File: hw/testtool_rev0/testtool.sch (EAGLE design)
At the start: 495 parts, among them IC1 SJA1105TELY, IC10 TJA1100HNZ, IC11 KSZ8061MNXI-TR, IC12 TJA1100HNZ, IC13 TLE9250XSJXUMA1, IC17 LP5907QMFX-3.3Q1, IC18 TLE9250XSJXUMA1, IC2 ATSAMV71Q21B-AABT, IC3 TJA1100HNZ, IC4 FT2232HL, IC5 TRS3232EQPWRQ1, IC6 SST26VF032BT-104I_SM, IC7 DS3231SN#, IC8 74HC7541D-Q100J, IC9 TPS62242DRVR, J10 5-2337992-3, J11 2301843-1, J12 1017505, J13 2301843-1, J15 693022010811, J2 2305018-2, J27 2041119-2, J3 1017505, J4 1017505, J5 1017505, J6 1017505, J7 1017505, J8 1017505, J9 1017505, U1 122-2920-GR, U2 LM63625, U3 TPS62007-Q1_DGS_10, Y1 NX3225SA-25MHZ-EXS00A-CS11338, Y3 ABM8AIG-12.000MHZ-1Z-T

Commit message: Add schematic for test tool based on the full vehicle control module design
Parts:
- removed C104: 10uF, rcl:C-USC0805
- removed C108, C111, C114, C116, C118, C120, C122, C124, C126, C128, C130, C132, C134, C136, C138, C140, C142, C144, C148, C149, C150, C151, C152, C153, C154, C155: 0.01uF, rcl:C-USC0603
- removed C109, C35, C36, C38, C42, C51, C52, C54, C58, C64, C65, C96: 1uF, rcl:C-USC0603
- removed C110, C21, C24, C26, C27, C29, C79, C80, C81, C82, C89: 0.1uF, rcl:C-USC0603
- removed C112, C113, C115, C117, C119, C121, C123, C125, C127, C129, C131, C133, C135, C137, C139, C141, C143, C145: 150nF, rcl:C-USC0603
- removed C22: 1000pF, rcl:C-USC0603
- removed C23, C25, C28, C32, C34, C39, C48, C50, C55: 10uF, rcl:C-USC0603
- removed C33, C37, C40, C41, C45, C46, C49, C53, C56, C57, C61, C62, C98: 100nF, rcl:C-USC0603
- removed C43, C44, C59, C60: 47pF, rcl:C-USC0603
- removed C47, C63: 4.7nF, rcl:C-USC0603
- removed C97: UCZ1K151MNQ1MS, samacsys:UCZ1K151MNQ1MS
- removed D10, D11, D12, D13, D14, D15, D16, D17, D18, D19, D20, D21, D22, D23, D24, D25, D26, D27, D28, D29, D30, D31, D32, D33, D34, D35: BAT54SWFILMY, samacsys:BAT54SWFILMY
- removed D2, D3: PESD2ETH-AXR, samacsys:PESD2ETH-AXR
- removed FL10, FL11, FL12, FL6, FL7, FL8: BLM18PG330SN1D, samacsys:BLM18PG330SN1D
- removed FL5, FL9: ACT45L-201-2P-TL000, samacsys:ACT45L-201-2P-TL000
- removed IC10, IC12: TJA1100HNZ, samacsys:TJA1100HNZ
- removed IC11: KSZ8061MNXI-TR, samacsys:KSZ8061MNXI-TR
- removed IC17: LP5907QMFX-3.3Q1, samacsys:LP5907QMFX-3.3Q1
- removed IC5: TRS3232EQPWRQ1, samacsys:TRS3232EQPWRQ1
- removed IC6: SST26VF032BT-104I_SM, samacsys:SST26VF032BT-104I_SM
- removed IC7: DS3231SN#, samacsys:DS3231SN#
- removed IC8: 74HC7541D-Q100J, samacsys:74HC7541D-Q100J
- removed IC9: TPS62242DRVR, samacsys:TPS62242DRVR
- removed J10: 5-2337992-3, samacsys:5-2337992-3
- removed J11, J13: 2301843-1, samacsys:2301843-1
- removed J12, J7, J8, J9: 1017505, samacsys:1017505
- removed J15: 693022010811, samacsys:693022010811
- removed J27: 2041119-2, samacsys:2041119-2
- removed L10: LPS3015-222MRB, samacsys:LPS3015-222MRB
- removed L3, L4, L5, L6: 0603CS-R12XGLU, samacsys:0603CS-R12XGLU
- removed LED10, LED2, LED3, LED8, LED9: (no value), led:LEDCHIPLED_0603
- removed R100, R101, R102, R199, R36, R38, R42, R45, R47, R49, R58, R60, R64, R67, R69, R71, R84, R93: 10k, rcl:R-US_R0603
- removed R105, R106, R115, R120, R125, R130, R135, R140, R145, R150, R155, R160, R165, R170, R175, R180, R185, R190: 4, rcl:R-US_R1206
- removed R107, R110, R111, R113, R114, R116, R119, R121, R123, R124, R126, R129, R131, R133, R134, R136, R139, R141, R143, R144, R146, R149, R151, R153, R154, R156, R159, R161, R163, R164, R166, R169, R171, R173, R174, R176, R179, R181, R184, R186, R189, R191, R194, R198, R79, R80, R81: 4.7k, rcl:R-US_R0603
- removed R108, R112, R117, R122, R127, R132, R137, R142, R147, R152, R157, R162, R167, R172, R177, R182, R187, R192: 2.74k, rcl:R-US_R0603
- removed R109, R118, R128, R138, R148, R158, R168, R178, R55, R77: 100k, rcl:R-US_R0603
- removed R27, R28, R29: 75, rcl:R-US_R0603
- removed R30, R33, R35, R53, R54, R57, R75, R76: 1k, rcl:R-US_R0603
- removed R34, R50, R51, R52, R56, R72, R73, R74: 49.9, rcl:R-US_R0603
- removed R37, R39, R43, R44, R46, R48, R59, R61, R65, R66, R68, R70: DNP, rcl:R-US_R0603
- removed R40, R62: 5.11k, rcl:R-US_R0603
- removed R41, R63, R78, R99: 0, rcl:R-US_R0603
- removed R94: 1.21k, rcl:R-US_R0603
- removed U1: 122-2920-GR, samacsys:122-2920-GR
- removed U?1, U?10, U?11, U?12, U?13, U?14, U?15, U?16, U?17, U?18, U?2, U?3, U?4, U?5, U?6, U?7, U?8, U?9: (no value), BTS50015-1TAD:BTS50015-1TAD
- added J1: 2305018-2, 2305018-2:2305018-2
- C17: value 1uF -> 100nF
- C18: value 8.2pF -> 10uF; device rcl:C-USC0603 -> rcl:C-USC0805
- C20: value 0.1uF -> 8.2pF
- IC1: value SJA1105TELY -> SST26VF032BT-104I_SM; device samacsys:SJA1105TELY -> samacsys:SST26VF032BT-104I_SM
- J3, J4, J5, J6: value 1017505 -> TBL009-254-04GY-2GY; device samacsys:1017505 -> samacsys:TBL009-254-04GY-2GY
- R10, R25: value 0 -> 10k
- R11, R14: value 10k -> DNP
- R12, R13: value DNP -> 10k
- R26: value 75 -> 0
- R31: value 6.04k -> 5.11k
- R32: value 4.7k -> 5.11k
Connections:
- net PHY1_CONFIG0 renamed PHY_CONFIG0
- net PHY1_CONFIG1 renamed PHY_CONFIG1
- net PHY1_TRX_M renamed PHY_TRX_M
- net PHY1_TRX_P renamed PHY_TRX_P
- removed net 3V3_AD_REF: C109.1, IC17.OUT, IC2.VREFP, R100.1
- removed net ADC0_0: C89.1, IC2.PD30, R93.2, R94.2
- removed net ADC0_1: IC2.PA21
- removed net ADC0_10: C140.1, D25.A,K, IC2.PB0, R181.2
- removed net ADC0_3: C128.1, D19.A,K, IC2.PE5, R151.2
- removed net ADC0_4: C130.1, D20.A,K, IC2.PE4, R156.2
- removed net ADC0_6: C132.1, D21.A,K, IC2.PA17, R161.2
- removed net ADC0_7: C134.1, D22.A,K, IC2.PA18, R166.2
- removed net ADC0_8: C136.1, D23.A,K, IC2.PA19, R171.2
- removed net ADC0_9: C138.1, D24.A,K, IC2.PA20, R176.2
- removed net ADC1_0: C142.1, D26.A,K, IC2.PB1, R186.2
- removed net ADC1_1: C144.1, D27.A,K, IC2.PC13, R191.2
- removed net ADC1_10: C124.1, D17.A,K, IC2.PE3, R141.2
- removed net ADC1_11: C126.1, D18.A,K, IC2.PE0, R146.2
- removed net ADC1_2: C111.1, D10.A,K, IC2.PC15, R107.2
- removed net ADC1_4: C108.1, D11.A,K, IC2.PC29, R111.2
- removed net ADC1_5: C114.1, D12.A,K, IC2.PC30, R116.2
- removed net ADC1_6: C116.1, D13.A,K, IC2.PC31, R121.2
- removed net ADC1_7: C118.1, D14.A,K, IC2.PC26, R126.2
- removed net ADC1_8: C120.1, D15.A,K, IC2.PC27, R131.2
- removed net ADC1_9: C122.1, D16.A,K, IC2.PC0, R136.2
- removed net CON_ETH1_TRX_M: C14.2, R22.2
- removed net CON_ETH1_TRX_P: C15.2, R23.2
- removed net CON_ETH2_TRX_M: C45.2, R53.2
- removed net CON_ETH2_TRX_P: C46.2, R54.2
- removed net CON_ETH3_TRX_M: C61.2, R75.2
- removed net CON_ETH3_TRX_P: C62.2, R76.2
- removed net DEBUG_ETH_CONFIG1: IC11.CRS, R32.2
- removed net DEBUG_ETH_LED0: IC11.LED0/TXER, R30.1
- removed net DEBUG_ETH_LED1: IC11.SIGDET, R33.1
- removed net DEBUG_ETH_RXM: IC11.RXM, J10.P6
- removed net DEBUG_ETH_RXP: IC11.RXP, J10.P3
- removed net DEBUG_ETH_TXM: IC11.TXM, J10.P2
- removed net DEBUG_ETH_TXP: IC11.TXP, J10.P1
- removed net EXTINT_RTC: IC2.PA0, IC7.!INT!/SQW, R81.1
- removed net EXT_DINPUT_0: R198.1
- removed net EXT_DINPUT_1: R113.1
- removed net EXT_DINPUT_2: R123.1
- removed net EXT_DINPUT_3: R133.1
- removed net EXT_DINPUT_4: R143.1
- removed net EXT_DINPUT_5: R153.1
- removed net EXT_DINPUT_6: R163.1
- removed net EXT_DINPUT_7: R173.1
- removed net EXT_PWR: D5.A, D9.A, TC1.5
- removed net HIGHSIDE_0_EN: IC2.PD11, R154.2
- removed net HIGHSIDE_0_OUTPUT: U?10.OUT1, U?10.OUT2, U?10.OUT3
- removed net HIGHSIDE_10_EN: IC2.PC2, R114.2
- removed net HIGHSIDE_10_OUTPUT: U?2.OUT1, U?2.OUT2, U?2.OUT3
- removed net HIGHSIDE_11_EN: IC2.PC3, R119.2
- removed net HIGHSIDE_11_OUTPUT: U?3.OUT1, U?3.OUT2, U?3.OUT3
- removed net HIGHSIDE_12_EN: IC2.PA16, R124.2
- removed net HIGHSIDE_12_OUTPUT: U?4.OUT1, U?4.OUT2, U?4.OUT3
- removed net HIGHSIDE_13_EN: IC2.PD27, R129.2
- removed net HIGHSIDE_13_OUTPUT: U?5.OUT1, U?5.OUT2, U?5.OUT3
- removed net HIGHSIDE_14_EN: IC2.PC7, R134.2
- removed net HIGHSIDE_14_OUTPUT: U?6.OUT1, U?6.OUT2, U?6.OUT3
- removed net HIGHSIDE_15_EN: IC2.PA15, R139.2
- removed net HIGHSIDE_15_OUTPUT: U?7.OUT1, U?7.OUT2, U?7.OUT3
- removed net HIGHSIDE_16_EN: IC2.PC6, R144.2
- removed net HIGHSIDE_16_OUTPUT: U?8.OUT1, U?8.OUT2, U?8.OUT3
- removed net HIGHSIDE_17_EN: IC2.PD24, R149.2
- removed net HIGHSIDE_17_OUTPUT: U?9.OUT1, U?9.OUT2, U?9.OUT3
- removed net HIGHSIDE_1_EN: IC2.PA2, R159.2
- removed net HIGHSIDE_1_OUTPUT: U?11.OUT1, U?11.OUT2, U?11.OUT3
- removed net HIGHSIDE_2_EN: IC2.PA25, R164.2
- removed net HIGHSIDE_2_OUTPUT: U?12.OUT1, U?12.OUT2, U?12.OUT3
- removed net HIGHSIDE_3_EN: IC2.PA7, R169.2
- removed net HIGHSIDE_3_OUTPUT: U?13.OUT1, U?13.OUT2, U?13.OUT3
- removed net HIGHSIDE_4_EN: IC2.PA31, R174.2
- removed net HIGHSIDE_4_OUTPUT: U?14.OUT1, U?14.OUT2, U?14.OUT3
- removed net HIGHSIDE_5_EN: IC2.PA8, R179.2
- removed net HIGHSIDE_5_OUTPUT: U?15.OUT1, U?15.OUT2, U?15.OUT3
- removed net HIGHSIDE_6_EN: IC2.PA23, R184.2
- removed net HIGHSIDE_6_OUTPUT: U?16.OUT1, U?16.OUT2, U?16.OUT3
- removed net HIGHSIDE_7_EN: IC2.PE1, R189.2
- removed net HIGHSIDE_7_OUTPUT: U?17.OUT1, U?17.OUT2, U?17.OUT3
- removed net HIGHSIDE_8_EN: IC2.PE2, R194.2
- removed net HIGHSIDE_8_OUTPUT: U?18.OUT1, U?18.OUT2, U?18.OUT3
- removed net HIGHSIDE_9_EN: IC2.PC1, R110.2
- removed net HIGHSIDE_9_OUTPUT: U?1.OUT1, U?1.OUT2, U?1.OUT3
- removed net I2C0_TWCK: IC2.PA4, IC7.SCL, R79.1
- removed net I2C0_TWD: IC2.PA3, IC7.SDA, R80.1
- removed net MII4_RXD0: IC1.MII4_RX0, IC11.RXD0
- removed net MII4_RXD1: IC1.MII4_RX1, IC11.RXD1
- removed net MII4_RXD2: IC1.MII4_RX2, IC11.RXD2
- removed net MII4_RXD3: IC1.MII4_RX3, IC11.RXD3
- removed net MII4_RXERR: IC11.RXERR
- removed net MII4_RX_CLK: IC1.MII4_RX_CLK, IC11.RXC
- removed net MII4_RX_DV: IC1.MII4_RX_DV, IC11.RXDV
- removed net MII4_RX_ER: IC1.MII4_RX_ER
- removed net MII4_TXD0: IC1.MII4_TXD0, IC11.TXD0
- removed net MII4_TXD1: IC1.MII4_TXD1, IC11.TXD1
- removed net MII4_TXD2: IC1.MII4_TXD2, IC11.TXD2
- removed net MII4_TXD3: IC1.MII4_TXD3, IC11.TXD3
- removed net MII4_TXEN: IC1.MII4_TXEN, IC11.TXEN
- removed net MII4_TX_CLK: IC1.MII3_TX_ER_1, IC11.TXC
- removed net MODEM_DISABLE: IC2.PB9, J27.W_DISABLE#
- removed net MODEM_RESET: IC2.PB8, J27.PERST#
- removed net MODEM_WAN_LED: J27.LED_WWAN#, LED9.C
- removed net N$100: C115.2, R115.1, U?3.GND
- removed net N$101: R116.1, R117.1, U?3.IS
- removed net N$102: C115.1, R119.1, U?3.IN
- removed net N$103: C117.2, R120.1, U?4.GND
- removed net N$104: R121.1, R122.1, U?4.IS
- removed net N$105: C117.1, R124.1, U?4.IN
- removed net N$106: C119.2, R125.1, U?5.GND
- removed net N$107: R126.1, R127.1, U?5.IS
- removed net N$108: C119.1, R129.1, U?5.IN
- removed net N$109: C121.2, R130.1, U?6.GND
- removed net N$110: R131.1, R132.1, U?6.IS
- removed net N$111: C121.1, R134.1, U?6.IN
- removed net N$112: C123.2, R135.1, U?7.GND
- removed net N$113: R136.1, R137.1, U?7.IS
- removed net N$114: C123.1, R139.1, U?7.IN
- removed net N$115: C125.2, R140.1, U?8.GND
- removed net N$116: R141.1, R142.1, U?8.IS
- removed net N$117: C125.1, R144.1, U?8.IN
- removed net N$118: C127.2, R145.1, U?9.GND
- removed net N$119: R146.1, R147.1, U?9.IS
- removed net N$12: IC3.XI, R10.2
- removed net N$120: C127.1, R149.1, U?9.IN
- removed net N$121: C129.2, R150.1, U?10.GND
- removed net N$122: R151.1, R152.1, U?10.IS
- removed net N$123: C129.1, R154.1, U?10.IN
- removed net N$124: C131.2, R155.1, U?11.GND
- removed net N$125: R156.1, R157.1, U?11.IS
- removed net N$126: C131.1, R159.1, U?11.IN
- removed net N$127: C133.2, R160.1, U?12.GND
- removed net N$128: R161.1, R162.1, U?12.IS
- removed net N$129: C133.1, R164.1, U?12.IN
- removed net N$130: C135.2, R165.1, U?13.GND
- removed net N$131: R166.1, R167.1, U?13.IS
- removed net N$132: C135.1, R169.1, U?13.IN
- removed net N$133: C137.2, R170.1, U?14.GND
- removed net N$134: R171.1, R172.1, U?14.IS
- removed net N$135: C137.1, R174.1, U?14.IN
- removed net N$136: C139.2, R175.1, U?15.GND
- removed net N$137: R176.1, R177.1, U?15.IS
- removed net N$138: C139.1, R179.1, U?15.IN
- removed net N$139: C141.2, R180.1, U?16.GND
- removed net N$140: R181.1, R182.1, U?16.IS
- removed net N$141: C141.1, R184.1, U?16.IN
- removed net N$142: C143.2, R185.1, U?17.GND
- removed net N$143: R186.1, R187.1, U?17.IS
- removed net N$144: C143.1, R189.1, U?17.IN
- removed net N$145: C145.2, R190.1, U?18.GND
- removed net N$146: R191.1, R192.1, U?18.IS
- removed net N$147: C145.1, R194.1, U?18.IN
- removed net N$148: C148.1, D29.A,K, IC8.A1, R113.2, R118.2
- removed net N$149: C149.1, D30.A,K, IC8.A2, R123.2, R128.2
- removed net N$150: C150.1, D31.A,K, IC8.A3, R133.2, R138.2
- removed net N$151: C151.1, D28.A,K, IC8.A0, R109.2, R198.2
- removed net N$152: C152.1, D32.A,K, IC8.A4, R143.2, R148.2
- removed net N$153: C153.1, D33.A,K, IC8.A5, R153.2, R158.2
- removed net N$154: C154.1, D34.A,K, IC8.A6, R163.2, R168.2
- removed net N$155: C155.1, D35.A,K, IC8.A7, R173.2, R178.2
- removed net N$21: C19.1, IC1.OSC_OUT, Y1.CRYSTAL_2
- removed net N$24: J10.ANODE_YELLOW, R33.2
- removed net N$25: C20.1, J10.P4
- removed net N$26: J10.P5, R26.2
- removed net N$27: C21.1, J10.P7
- removed net N$28: J10.P8, R27.2
- removed net N$29: LED2.C, R35.2
- removed net N$30: IC11.REXT, R31.2
- removed net N$31: IC10.WAKE/LED, R35.1
- removed net N$32: C36.1, IC10.VDDA(1V8)
- removed net N$33: C38.1, IC10.VDDD(1V8)
- removed net N$34: C34.1, C35.1, FL6.2, IC10.VDDA(3V3)
- removed net N$35: C32.1, C33.1, C37.1, FL7.2, IC10.VDDA(TX), IC10.VDDD(3V3)
- removed net N$36: C39.1, C40.1, C41.1, FL8.2, IC10.VDD(IO)_1, IC10.VDD(IO)_2
- removed net N$37: IC10.EN, R40.1
- removed net N$38: J10.ANODE_GREEN, R30.2
- removed net N$39: J10.P10, R28.2
- removed net N$40: J10.P9, R29.2
- removed net N$41: C22.1, R26.1, R27.1, R28.1, R29.1
- removed net N$42: IC10.XI, R41.2
- removed net N$44: D2.I/O_2, FL5.1, L4.2, R52.2
- removed net N$45: D2.I/O_1, FL5.2, L3.2, R50.2
- removed net N$46: C43.1, R34.2, R50.1
- removed net N$47: C44.1, R51.2, R52.1
- removed net N$48: C45.1, FL5.4
- removed net N$49: C46.1, FL5.3
- removed net N$50: C47.1, R53.1, R54.1, R55.2
- removed net N$51: LED3.C, R57.2
- removed net N$52: IC12.WAKE/LED, R57.1
- removed net N$53: C52.1, IC12.VDDA(1V8)
- removed net N$54: C54.1, IC12.VDDD(1V8)
- removed net N$55: C50.1, C51.1, FL10.2, IC12.VDDA(3V3)
- removed net N$56: C48.1, C49.1, C53.1, FL11.2, IC12.VDDA(TX), IC12.VDDD(3V3)
- removed net N$57: C55.1, C56.1, C57.1, FL12.2, IC12.VDD(IO)_1, IC12.VDD(IO)_2
- removed net N$58: IC12.EN, R62.1
- removed net N$59: IC12.XI, R63.2
- removed net N$60: D3.I/O_2, FL9.1, L6.2, R74.2
- removed net N$61: D3.I/O_1, FL9.2, L5.2, R72.2
- removed net N$62: C59.1, R56.2, R72.1
- removed net N$63: C60.1, R73.2, R74.1
- removed net N$64: C61.1, FL9.4
- removed net N$65: C62.1, FL9.3
- removed net N$66: C63.1, R75.1, R76.1, R77.2
- removed net N$75: C79.1, IC5.C1+
- removed net N$76: C79.2, IC5.C1-
- removed net N$77: C80.1, IC5.C2+
- removed net N$78: C80.2, IC5.C2-
- removed net N$79: C81.1, IC5.V-
- removed net N$88: LED8.A, R100.2
- removed net N$89: IC9.SW, L10.2
- removed net N$90: LED10.A, R101.2
- removed net N$92: LED9.A, R102.2
- removed net N$94: C112.2, R106.1, U?1.GND
- removed net N$95: R107.1, R108.1, U?1.IS
- removed net N$96: C113.2, R105.1, U?2.GND
- removed net N$97: C112.1, R110.1, U?1.IN
- removed net N$98: R111.1, R112.1, U?2.IS
- removed net N$99: C113.1, R114.1, U?2.IN
- removed net PHY2_CONFIG0: IC10.RXD2/CONFIG0, R36.1, R37.1
- removed net PHY2_CONFIG1: IC10.RXD3/CONFIG1, R38.1, R39.1
- removed net PHY2_TRX_M: IC10.TRX_M, L4.1, R51.1
- removed net PHY2_TRX_P: IC10.TRX_P, L3.1, R34.1
- removed net PHY3_CONFIG0: IC12.RXD2/CONFIG0, R58.1, R59.1
- removed net PHY3_CONFIG1: IC12.RXD3/CONFIG1, R60.1, R61.1
- removed net PHY3_TRX_M: IC12.TRX_M, L6.1, R73.1
- removed net PHY3_TRX_P: IC12.TRX_P, L5.1, R56.1
- removed net PHY_RESET: IC11.!RESET
- removed net PROT_DINPUT_0: IC2.PD29, IC8.Y0
- removed net PROT_DINPUT_1: IC2.PD15, IC8.Y1
- removed net PROT_DINPUT_2: IC2.PC17, IC8.Y2
- removed net PROT_DINPUT_3: IC2.PD10, IC8.Y3
- removed net PROT_DINPUT_4: IC2.PC16, IC8.Y4
- removed net PROT_DINPUT_5: IC2.PA1, IC8.Y5
- removed net PROT_DINPUT_6: IC2.PC14, IC8.Y6
- removed net PROT_DINPUT_7: IC2.PC11, IC8.Y7
- removed net RMII0_CRSDV: IC1.MII0_RX_DV, IC2.PD1
- removed net RMII0_REFCLK: IC1.MII0_TX_CLK, IC2.PD0
- removed net RMII0_RXD0: IC1.MII0_RX0, IC2.PD2
- removed net RMII0_RXD1: IC1.MII0_RX1, IC2.PD3
- removed net RMII0_TXD0: IC1.MII0_TXD0, IC2.PD5
- removed net RMII0_TXD1: IC1.MII0_TXD1, IC2.PD6
- removed net RMII0_TXEN: IC1.MII0_TXEN, IC2.PD4
- removed net RMII0_TXER: IC1.MII0_TX_ER, IC2.PD7
- removed net RMII1_CRSDV: IC1.MII1_RX_DV, IC3.RXDV/CONFIG2/CRSDV, R11.1, R12.1
- removed net RMII1_REFCLK: IC1.MII1_TX_CLK, IC3.RXC/REF_CLK
- removed net RMII1_RXD0: IC1.MII1_RX0, IC3.RXD0/PHYAD0, R15.1, R16.1
- removed net RMII1_RXD1: IC1.MII1_RX1, IC3.RXD1/PHYAD1, R17.1, R18.1
- removed net RMII1_RXER: IC1.MII1_RX_ER, IC3.RXER/CONFIG3, R13.1, R14.1
- removed net RMII1_TXD0: IC1.MII1_TXD0, IC3.TXD0
- removed net RMII1_TXD1: IC1.MII1_TXD1, IC3.TXD1
- removed net RMII1_TXEN: IC1.MII1_TXEN
- removed net RMII2_CRSDV: IC1.MII2_RX_DV, IC10.RXDV/CONFIG2/CRSDV, R42.1, R43.1
- removed net RMII2_REFCLK: IC1.MII2_RX_CLK_2, IC10.RXC/REF_CLK
- removed net RMII2_RXD0: IC1.MII2_RX0, IC10.RXD0/PHYAD0, R46.1, R47.1
- removed net RMII2_RXD1: IC1.MII2_RX1, IC10.RXD1/PHYAD1, R48.1, R49.1
- removed net RMII2_RXER: IC10.RXER/CONFIG3, R44.1, R45.1
- removed net RMII2_TXD0: IC1.MII2_TXD0, IC10.TXD0
- removed net RMII2_TXD1: IC1.MII2_TXD1, IC10.TXD1
- removed net RMII2_TXEN: IC1.MII2_TXEN
- removed net RMII3_CRSDV: IC1.MII3_RX_DV, IC12.RXDV/CONFIG2/CRSDV, R64.1, R65.1
- removed net RMII3_REFCLK: IC1.MII3_TX_CLK, IC12.RXC/REF_CLK
- removed net RMII3_RXD0: IC1.MII3_RX0, IC12.RXD0/PHYAD0, R68.1, R69.1
- removed net RMII3_RXD1: IC1.MII3_RX1, IC12.RXD1/PHYAD1, R70.1, R71.1
- removed net RMII3_RXER: IC12.RXER/CONFIG3, R66.1, R67.1
- removed net RMII3_TXD0: IC1.MII3_TXD0, IC12.TXD0
- removed net RMII3_TXD1: IC1.MII3_TXD1, IC12.TXD1
- removed net RMII3_TXEN: IC1.MII3_TXEN
- removed net RS232_PORT0_RX: IC5.RIN1, J11.2
- removed net RS232_PORT0_TX: IC5.DOUT1, J11.3
- removed net RS232_PORT1_RX: IC5.RIN2, J13.2
- removed net RS232_PORT1_TX: IC5.DOUT2, J13.3
- removed net RTC_RESET: IC2.PD13, IC7.!RST
- removed net SIM_CLK: J15.CLK, J27.UIM_CLK
- removed net SIM_DATA: J15.I/O, J27.UIM_DATA
- removed net SIM_PWR: J15.VCC, J15.VPP, J27.UIM_PWR
- removed net SIM_RESET: J15.RST, J27.UIM_RESET
- removed net SPI0_CS: IC1.SS_N, IC2.PD23
- removed net SPI0_MISO: IC1.SDO, IC2.PD20
- removed net SPI0_MOSI: IC1.SDI, IC2.PD21
- removed net SPI0_SCLK: IC1.SCK, IC2.PD22
- removed net SWITCH_REF_CLK: IC1.CLK_OUT, IC11.XI
- removed net UART2_RXD: IC2.PD25, IC5.ROUT1
- removed net UART2_TXD: IC2.PD26, IC5.DIN1
- removed net UART3_RXD: IC2.PD28, IC5.ROUT2
- removed net UART3_TXD: IC2.PD31, IC5.DIN2
- removed net VDD: C104.1, C25.1, C26.1, C27.1, C28.1, C29.1, IC1.VDDA_OSC, IC1.VDDA_PLL, IC1.VDD_CORE_1, IC1.VDD_CORE_2, IC1.VDD_CORE_3, IC1.VDD_CORE_4, IC1.VDD_CORE_5, IC1.VDD_CORE_6, IC1.VDD_CORE_7, IC1.VDD_CORE_8, IC11.AVDDL, IC11.VDDL_1, IC11.VDDL_2, IC9.FB, L10.1, R101.1
- new net CON_ETH_TRX_M: C14.2, J3.5, R22.2
- new net CON_ETH_TRX_P: C15.2, J3.3, R23.2
- new net PHY_XTAL_I: C19.1, IC3.XI, Y1.CRYSTAL_1
- new net PHY_XTAL_O: C20.1, IC3.XO, Y1.CRYSTAL_2
- new net RMII_CRSDV: IC2.PD4, IC3.RXDV/CONFIG2/CRSDV, R11.1, R12.1
- new net RMII_REFCLK: IC2.PD0, IC3.RXC/REF_CLK
- new net RMII_RXD0: IC2.PD5, IC3.RXD0/PHYAD0, R15.1, R16.1
- new net RMII_RXD1: IC2.PD6, IC3.RXD1/PHYAD1, R17.1, R18.1
- new net RMII_RXER: IC2.PD7, IC3.RXER/CONFIG3, R13.1, R14.1
- new net RMII_TXD0: IC2.PD2, IC3.TXD0
- new net RMII_TXD1: IC2.PD3, IC3.TXD1
- new net RMII_TXEN: IC2.PD1, IC3.TXEN
- new net VUSB: D5.A, D9.A, J1.VBUS_A, J1.VBUS_B
- net +3V3: now also C17.1, IC1.HOLD/SIO3, IC1.VDD, IC2.VREFP, J6.1, J6.3; no longer C23.1, C24.1, C42.1, C58.1, C64.1, C82.1, C96.1, C97.+, C98.1, D10.K, D11.K, D12.K, D13.K, D14.K, D15.K, D16.K, D17.K, D18.K, D19.K, D2.VCC, D20.K, D21.K, D22.K, D23.K, D24.K, D25.K, D26.K, D27.K, D28.A, D29.A, D3.VCC, D30.A, D31.A, D32.A, D33.A, D34.A, D35.A, FL10.1, FL11.1, FL12.1, FL6.1, FL7.1, FL8.1, IC1.VDDIO_CLO, IC1.VDDIO_HOST, IC1.VDDIO_MII0_1, IC1.VDDIO_MII0_2, IC1.VDDIO_MII0_3, IC1.VDDIO_MII1_1, IC1.VDDIO_MII1_2, IC1.VDDIO_MII1_3, IC1.VDDIO_MII2_1, IC1.VDDIO_MII2_2, IC1.VDDIO_MII2_3, IC1.VDDIO_MII3_1, IC1.VDDIO_MII3_3, IC1.VDDIO_MII4_1, IC1.VDDIO_MII4_2, IC1.VDDIO_MII4_3, IC10.VBAT, IC11.AVDDH, IC11.VDDIO, IC12.VBAT, IC5.VCC, IC6.HOLD/SIO3, IC6.VDD, IC7.VCC, IC8.VCC, J27.+3.3VAUX_1, J27.+3.3VAUX_2, J27.+3.3VAUX_3, J27.+3.3VAUX_4, J27.3.3VAUX, LED2.A, LED3.A, R102.1, R32.1, R36.2, R38.2, R40.2, R42.2, R44.2, R46.2, R48.2, R58.2, R60.2, R62.2, R64.2, R66.2, R68.2, R70.2, R78.2, R79.2, R80.2, R81.2
- net +5V: now also C18.1, J6.5, J6.7, U3.EN; no longer C110.1, IC17.IN, IC9.VIN
- net 3V3_SUPPLY_PGOOD: now also R26.1; no longer R99.1
- net 5V_SUPPLY_PGOOD: no longer IC17.EN, IC9.EN, U3.EN
- net CAN0_H: now also J4.1
- net CAN0_L: now also J4.3
- net CAN1_H: now also J4.5
- net CAN1_L: now also J4.7
- net ETH_MDC: no longer IC10.MDC, IC11.MDC, IC12.MDC
- net ETH_MDIO: no longer IC10.MDIO, IC11.MDIO, IC12.MDIO
- net FLASH_WP: now also IC1.WP#/SIO2, R25.1; no longer IC2.PC4, IC6.WP#/SIO2, R78.1
- net GND: now also C17.2, IC1.VSS, J1.GND, J1.GNDA, J1.GNDB, J1.SHIELD, J3.1, J3.7, J5.5, J5.7, R10.2, R25.2, R32.1; no longer C104.2, C108.2, C109.2, C110.2, C111.2, C114.2, C116.2, C118.2, C120.2, C122.2, C124.2, C126.2, C128.2, C130.2, C132.2, C134.2, C136.2, C138.2, C140.2, C142.2, C144.2, C148.2, C149.2, C150.2, C151.2, C152.2, C153.2, C154.2, C155.2, C21.2, C22.2, C23.2, C24.2, C25.2, C26.2, C27.2, C28.2, C29.2, C32.2, C33.2, C34.2, C35.2, C36.2, C37.2, C38.2, C39.2, C40.2, C41.2, C42.2, C43.2, C44.2, C47.2, C48.2, C49.2, C50.2, C51.2, C52.2, C53.2, C54.2, C55.2, C56.2, C57.2, C58.2, C59.2, C60.2, C63.2, C64.2, C81.2, C82.2, C89.2, C96.2, C97.-, C98.2, D10.A, D11.A, D12.A, D13.A, D14.A, D15.A, D16.A, D17.A, D18.A, D19.A, D2.GND, D20.A, D21.A, D22.A, D23.A, D24.A, D25.A, D26.A, D27.A, D28.K, D29.K, D3.GND, D30.K, D31.K, D32.K, D33.K, D34.K, D35.K, IC1.VSSA_OSC, IC1.VSSA_PLL, IC1.VSS_1, IC1.VSS_10, IC1.VSS_11, IC1.VSS_12, IC1.VSS_13, IC1.VSS_14, IC1.VSS_15, IC1.VSS_16, IC1.VSS_17, IC1.VSS_18, IC1.VSS_19, IC1.VSS_2, IC1.VSS_20, IC1.VSS_21, IC1.VSS_22, IC1.VSS_23, IC1.VSS_24, IC1.VSS_25, IC1.VSS_26, IC1.VSS_27, IC1.VSS_28, IC1.VSS_29, IC1.VSS_3, IC1.VSS_30, IC1.VSS_31, IC1.VSS_32, IC1.VSS_33, IC1.VSS_34, IC1.VSS_35, IC1.VSS_36, IC1.VSS_37, IC1.VSS_38, IC1.VSS_39, IC1.VSS_4, IC1.VSS_40, IC1.VSS_41, IC1.VSS_42, IC1.VSS_43, IC1.VSS_44, IC1.VSS_45, IC1.VSS_5, IC1.VSS_6, IC1.VSS_7, IC1.VSS_8, IC1.VSS_9, IC10.GND_1, IC10.GND_2, IC10.GND_3, IC10.GND_4, IC10.TXER, IC11.PADDLE, IC12.GND_1, IC12.GND_2, IC12.GND_3, IC12.GND_4, IC12.TXER, IC17.GND, IC5.GND, IC6.VSS, IC7.GND, IC7.NC_1, IC7.NC_2, IC7.NC_3, IC7.NC_4, IC7.NC_5, IC7.NC_6, IC7.NC_7, IC7.NC_8, IC8.!OE1, IC8.!OE2, IC8.GND, IC9.EP, IC9.GND, IC9.MODE, J10.CATHODE_GREEN, J10.CATHODE_YELLOW, J10.MH1, J10.MH2, J11.5, J11.MH1, J11.MH2, J13.5, J13.MH1, J13.MH2, J15.GND, J27.GND_1, J27.GND_10, J27.GND_11, J27.GND_12, J27.GND_13, J27.GND_14, J27.GND_2, J27.GND_3, J27.GND_4, J27.GND_5, J27.GND_6, J27.GND_7, J27.GND_8, J27.GND_9, J27.RESERVED_1, LED10.C, LED8.C, R10.1, R105.2, R106.2, R108.2, R109.1, R112.2, R115.2, R117.2, R118.1, R120.2, R122.2, R125.2, R127.2, R128.1, R130.2, R132.2, R135.2, R137.2, R138.1, R140.2, R142.2, R145.2, R147.2, R148.1, R150.2, R152.2, R155.2, R157.2, R158.1, R160.2, R162.2, R165.2, R167.2, R168.1, R170.2, R172.2, R175.2, R177.2, R178.1, R180.2, R182.2, R185.2, R187.2, R190.2, R192.2, R199.2, R37.2, R39.2, R41.1, R43.2, R45.2, R47.2, R49.2, R55.1, R59.2, R61.2, R63.1, R65.2, R67.2, R69.2, R71.2, R77.1, R94.1, U1.3
- net HOST_RESET: now also R26.2; no longer R99.2
- net HOST_USB_DM: now also J1.DA_N, J1.DB_N; no longer J27.USB_D-
- net HOST_USB_DP: now also J1.DA_P, J1.DB_P; no longer J27.USB_D+
- net N$1: now also J1.CC1, R31.2; no longer IC7.VBAT, U1.1, U1.2
- net N$20: now also J1.CC2, R32.2; no longer C18.1, IC1.OSC_IN, Y1.CRYSTAL_1
- net PHY_RST: now also R10.1; no longer IC10.RST_N, IC12.RST_N, R199.1
- net QSPI_QCS: now also IC1.CE#; no longer IC6.CE#
- net QSPI_QIO0: now also IC1.SI/SIO0; no longer IC6.SI/SIO0
- net QSPI_QIO1: now also IC1.SO/SIO1; no longer IC6.SO/SIO1
- net QSPI_QSCK: now also IC1.SCK; no longer IC6.SCK
- net SWITCHED_IGN: now also J5.3
- net VBATT: now also J5.1; no longer U?1.VS, U?10.VS, U?11.VS, U?12.VS, U?13.VS, U?14.VS, U?15.VS, U?16.VS, U?17.VS, U?18.VS, U?2.VS, U?3.VS, U?4.VS, U?5.VS, U?6.VS, U?7.VS, U?8.VS, U?9.VS
- net VBATT_PROT: no longer R93.1
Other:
- note added: "3. Debug UART"
- note added: "4. Ethernet PHY"
- note added: "5. CAN"
- note added: "6. Connectors"
- note added: "CONFIG2"
- note added: "CONFIG3"
- note added: "CONFIG3/2: 0/0 = Normal MII 0/1 = RMII mode (external 50 MHz oscillator) 1/0 = RMII mode (25 MHz crystal) 1/1 = Reverse MII mode"
- note added: "Connection of USB should also enable the board"
- note added: "PHYADDR0"
- note added: "PHYADDR1"
- note added: "Test Tool"
- note removed: "10. High Side Drivers (1/2)"
- note removed: "10. High-side drivers (1/2)"
- note removed: "11. High Side Drivers (2/2)"
- note removed: "11. High-side drivers (2/2)"
- note removed: "12. CAN"
- note removed: "13. Modem"
- note removed: "14. Digital Input"
- note removed: "14. Digital Inputs"
- note removed: "15. Connectors"
- note removed: "1V2 for Ethernet Switch"
- note removed: "3. RS232 and Debug UART"
- note removed: "3V3 for analog reference"
- note removed: "4. External Flash and RTC"
- note removed: "5. Ethernet Switch"
- note removed: "6. Ethernet PHY 1"
- note removed: "7. Ethernet PHY 2"
- note removed: "8. Ethernet PHY 3"
- note removed: "9. Ethernet PHY 4"
- note removed: "9. Ethernet PHY 4 (100BASE-TX)"
- note removed: "Connection of JTAG should also enable the board"
- note removed: "Green LED = Serial Link is Up Yellow LED = Signal Detected"
- note removed: "MicroSIM socket"
- note removed: "RC cutoff ~160Hz"
- note removed: "RC lowpass on IS results in ~3400Hz cutoff"
- note removed: "Vehicle Control Module"

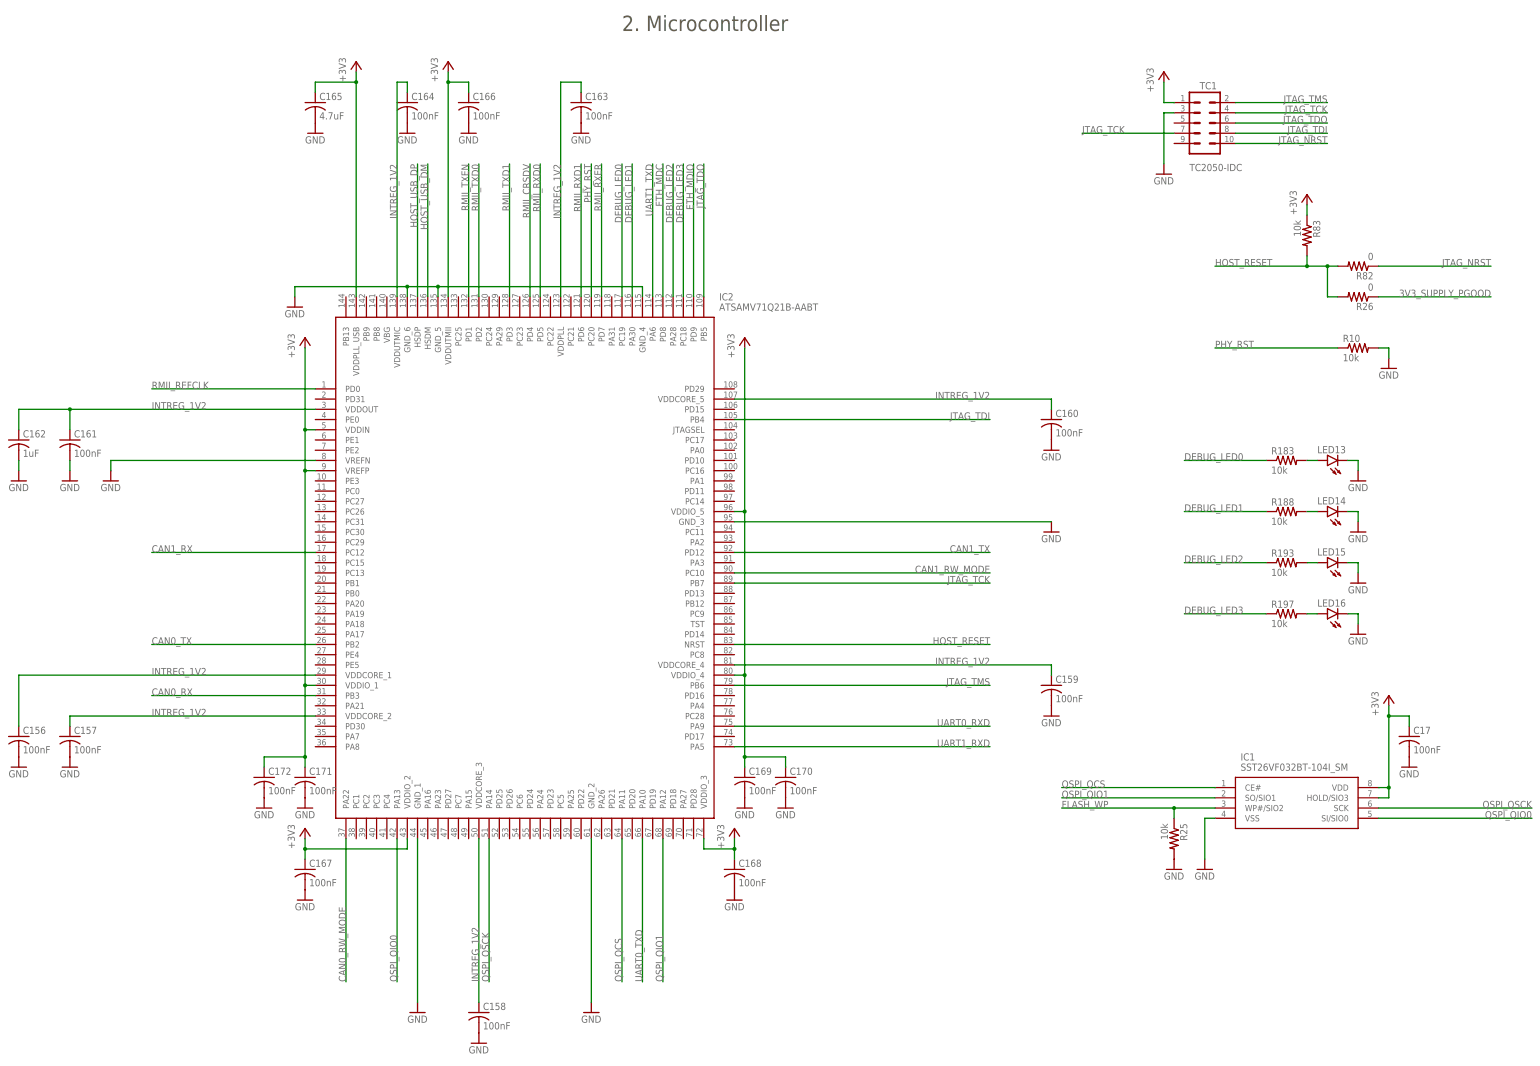
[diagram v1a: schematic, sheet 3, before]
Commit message: Add missing oscillator, start to layout testtool board
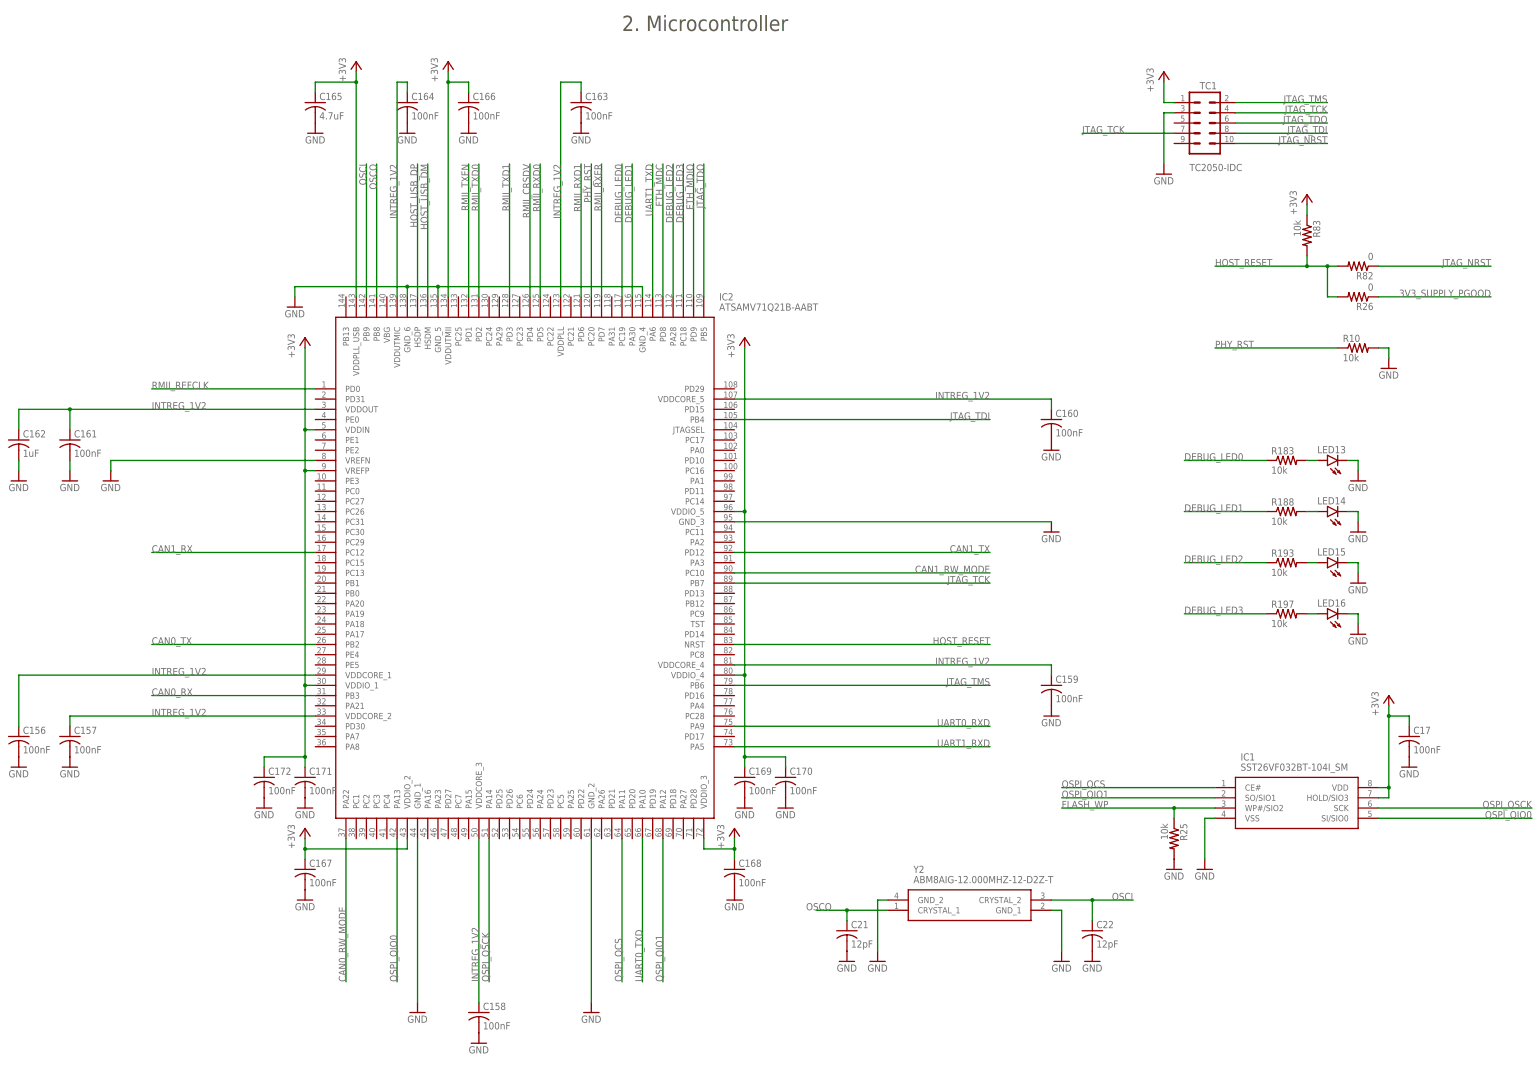
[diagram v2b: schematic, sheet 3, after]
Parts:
- added C21, C22: 12pF, rcl:C-USC0603
- added Y2: ABM8AIG-12.000MHZ-12-D2Z-T, samacsys:ABM8AIG-12.000MHZ-12-D2Z-T
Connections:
- new net OSCI: C22.1, IC2.PB9, Y2.CRYSTAL_2
- new net OSCO: C21.1, IC2.PB8, Y2.CRYSTAL_1
- net GND: now also C21.2, C22.2, Y2.GND_1, Y2.GND_2
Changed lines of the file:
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@@
 <part name="GND40" library="supply1" library_urn="urn:adsk.eagle:library:371" deviceset="GND" device=""/>
 <part name="R26" library="rcl" library_urn="urn:adsk.eagle:library:334" deviceset="R-US_" device="R0603" package3d_urn="urn:adsk.eagle:package:23555/3" value="0"/>
+<part name="Y2" library="samacsys" deviceset="ABM8AIG-12.000MHZ-12-D2Z-T" device=""/>
+<part name="C21" library="rcl" library_urn="urn:adsk.eagle:library:334" deviceset="C-US" device="C0603" package3d_urn="urn:adsk.eagle:package:23616/2" value="12pF"/>
+<part name="C22" library="rcl" library_urn="urn:adsk.eagle:library:334" deviceset="C-US" device="C0603" package3d_urn="urn:adsk.eagle:package:23616/2" value="12pF"/>
+<part name="GND41" library="supply1" library_urn="urn:adsk.eagle:library:371" deviceset="GND" device=""/>
+<part name="GND42" library="supply1" library_urn="urn:adsk.eagle:library:371" deviceset="GND" device=""/>
+<part name="GND43" library="supply1" library_urn="urn:adsk.eagle:library:371" deviceset="GND" device=""/>
+<part name="GND44" library="supply1" library_urn="urn:adsk.eagle:library:371" deviceset="GND" device=""/>
 </parts>
 <sheets>
@@
 <attribute name="VALUE" x="372.11" y="201.422" size="1.778" layer="96" rot="R180"/>
 </instance>
+<instance part="Y2" gate="G$1" x="251.46" y="48.26" smashed="yes">
+<attribute name="NAME" x="257.81" y="55.88" size="1.778" layer="95" align="center-left"/>
+<attribute name="VALUE" x="257.81" y="53.34" size="1.778" layer="96" align="center-left"/>
+</instance>
+<instance part="C21" gate="G$1" x="241.3" y="40.64" smashed="yes">
+<attribute name="NAME" x="242.316" y="41.275" size="1.778" layer="95"/>
+<attribute name="VALUE" x="242.316" y="36.449" size="1.778" layer="96"/>
+</instance>
+<instance part="C22" gate="G$1" x="302.26" y="40.64" smashed="yes">
+<attribute name="NAME" x="303.276" y="41.275" size="1.778" layer="95"/>
+<attribute name="VALUE" x="303.276" y="36.449" size="1.778" layer="96"/>
+</instance>
+<instance part="GND41" gate="1" x="241.3" y="33.02" smashed="yes">
+<attribute name="VALUE" x="238.76" y="30.48" size="1.778" layer="96"/>
+</instance>
+<instance part="GND42" gate="1" x="302.26" y="33.02" smashed="yes">
+<attribute name="VALUE" x="299.72" y="30.48" size="1.778" layer="96"/>
+</instance>
+<instance part="GND43" gate="1" x="248.92" y="33.02" smashed="yes">
+<attribute name="VALUE" x="246.38" y="30.48" size="1.778" layer="96"/>
+</instance>
+<instance part="GND44" gate="1" x="294.64" y="33.02" smashed="yes">
+<attribute name="VALUE" x="292.1" y="30.48" size="1.778" layer="96"/>
+</instance>
 </instances>
 <busses>
@@
 <pinref part="GND40" gate="1" pin="GND"/>
 </segment>
+<segment>
+<pinref part="C21" gate="G$1" pin="2"/>
+<pinref part="GND41" gate="1" pin="GND"/>
+</segment>
+<segment>
+<pinref part="C22" gate="G$1" pin="2"/>
+<pinref part="GND42" gate="1" pin="GND"/>
+</segment>
+<segment>
+<pinref part="Y2" gate="G$1" pin="GND_2"/>
+<wire x1="251.46" y1="48.26" x2="248.92" y2="48.26" width="0.1524" layer="91"/>
+<pinref part="GND43" gate="1" pin="GND"/>
+<wire x1="248.92" y1="48.26" x2="248.92" y2="35.56" width="0.1524" layer="91"/>
+</segment>
+<segment>
+<pinref part="Y2" gate="G$1" pin="GND_1"/>
+<wire x1="292.1" y1="45.72" x2="294.64" y2="45.72" width="0.1524" layer="91"/>
+<pinref part="GND44" gate="1" pin="GND"/>
+<wire x1="294.64" y1="45.72" x2="294.64" y2="35.56" width="0.1524" layer="91"/>
+</segment>
 </net>
 <net name="CAN0_RW_MODE" class="0">
@@
 </segment>
 </net>
+<net name="OSCO" class="0">
+<segment>
+<pinref part="Y2" gate="G$1" pin="CRYSTAL_1"/>
+<wire x1="251.46" y1="45.72" x2="241.3" y2="45.72" width="0.1524" layer="91"/>
+<pinref part="C21" gate="G$1" pin="1"/>
+<wire x1="241.3" y1="45.72" x2="233.68" y2="45.72" width="0.1524" layer="91"/>
+<wire x1="241.3" y1="43.18" x2="241.3" y2="45.72" width="0.1524" layer="91"/>
+<junction x="241.3" y="45.72"/>
+<label x="231.14" y="45.72" size="1.778" layer="95"/>
+</segment>
+<segment>
+<pinref part="IC2" gate="G$1" pin="PB8"/>
+<wire x1="124.46" y1="198.12" x2="124.46" y2="231.14" width="0.1524" layer="91"/>
+<label x="124.46" y="231.14" size="1.778" layer="95" rot="MR270"/>
+</segment>
+</net>
+<net name="OSCI" class="0">
+<segment>
+<pinref part="Y2" gate="G$1" pin="CRYSTAL_2"/>
+<wire x1="292.1" y1="48.26" x2="302.26" y2="48.26" width="0.1524" layer="91"/>
+<pinref part="C22" gate="G$1" pin="1"/>
+<wire x1="302.26" y1="48.26" x2="312.42" y2="48.26" width="0.1524" layer="91"/>
+<wire x1="302.26" y1="43.18" x2="302.26" y2="48.26" width="0.1524" layer="91"/>
+<junction x="302.26" y="48.26"/>
+<label x="312.42" y="48.26" size="1.778" layer="95" rot="MR0"/>
+</segment>
+<segment>
+<pinref part="IC2" gate="G$1" pin="PB9"/>
+<wire x1="121.92" y1="198.12" x2="121.92" y2="231.14" width="0.1524" layer="91"/>
+<label x="121.92" y="231.14" size="1.778" layer="95" rot="MR270"/>
+</segment>
+</net>
